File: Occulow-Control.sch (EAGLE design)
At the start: 39 parts, among them T1 DMP3010LK3, T2 DMP3010LK3, T3 DMP3010LK3

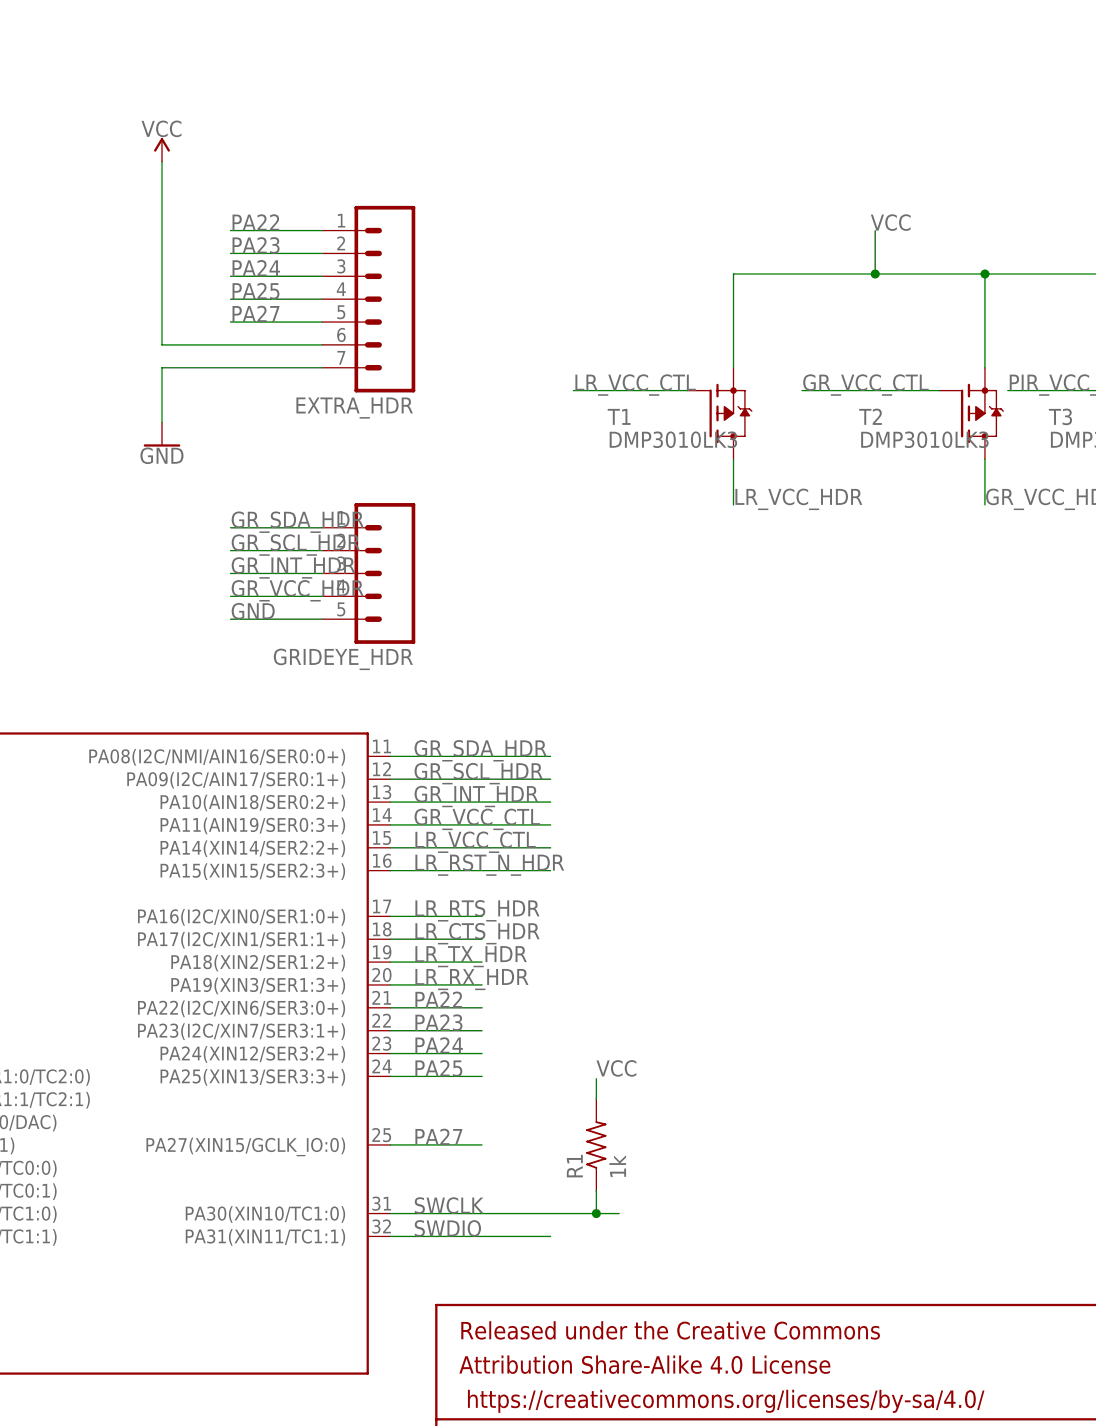
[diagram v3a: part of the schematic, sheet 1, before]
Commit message: Added LED status, bom. Fixes #6"
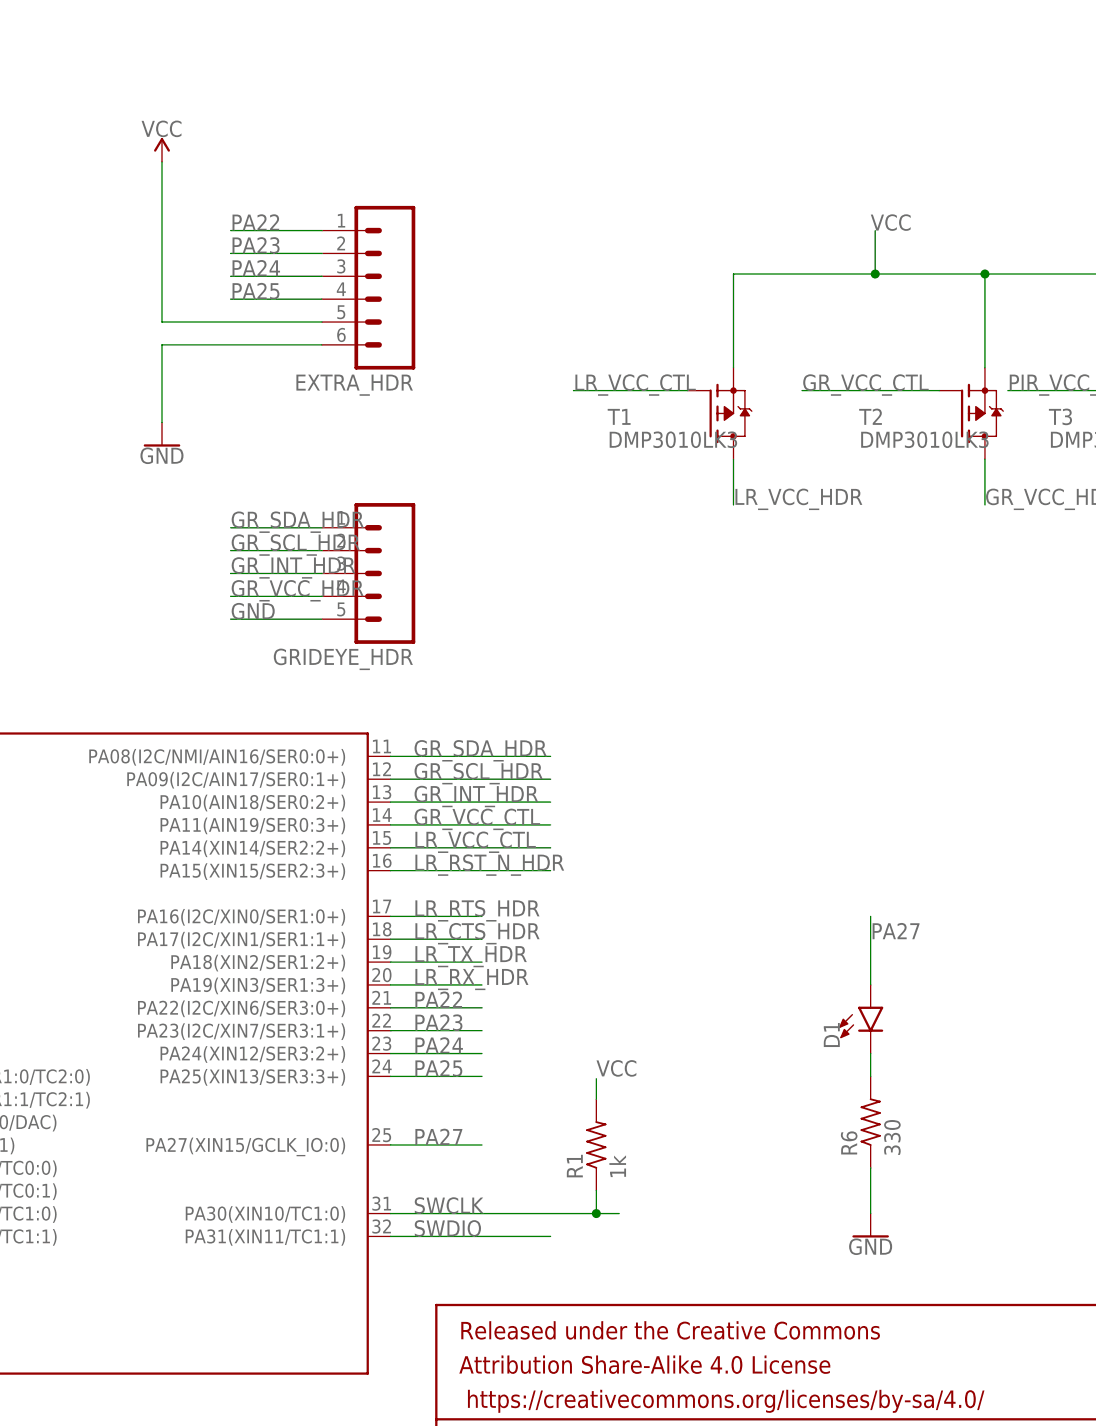
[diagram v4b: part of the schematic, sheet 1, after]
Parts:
- added D1: (no value), SparkFun-LED:LED1206
- added R6: 330, resistor:R-US_R1206
- EXTRA_HDR: device con-amp-quick:M07 -> con-amp-quick:M06
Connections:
- new net N$1: D1.C, R6.2
- net GND: now also EXTRA_HDR.6, R6.1; no longer EXTRA_HDR.7
- net PA27: now also D1.A; no longer EXTRA_HDR.5
- net VCC: now also EXTRA_HDR.5; no longer EXTRA_HDR.6
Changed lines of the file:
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@@
 <part name="SUPPLY6" library="SparkFun-PowerSymbols" deviceset="VCC" device=""/>
 <part name="GND11" library="SparkFun-PowerSymbols" deviceset="GND" device=""/>
-<part name="EXTRA_HDR" library="con-amp-quick" deviceset="M07" device=""/>
+<part name="EXTRA_HDR" library="con-amp-quick" deviceset="M06" device=""/>
 <part name="L1" library="resistor" deviceset="L-US" device="L3225M" value="10uH"/>
 <part name="L2" library="SparkFun-Coils" deviceset="FERRITE_BEAD" device="-0603" value=""/>
@@
 <part name="FRAME3" library="SparkFun-Aesthetics" deviceset="FRAME-LETTER" device="NO_PACKAGE"/>
 <part name="U$5" library="cortex-debug" deviceset="CORTEX-ICE" device=""/>
+<part name="D1" library="SparkFun-LED" deviceset="LED" device="1206"/>
+<part name="R6" library="resistor" deviceset="R-US_" device="R1206" value="330"/>
+<part name="GND5" library="SparkFun-PowerSymbols" deviceset="GND" device=""/>
 </parts>
 <sheets>
@@
 <instance part="LR_CTL_HDR" gate="G$1" x="63.5" y="142.24"/>
 <instance part="U$5" gate="G$1" x="66.04" y="116.84"/>
+<instance part="D1" gate="G$1" x="195.58" y="68.58"/>
+<instance part="R6" gate="G$1" x="195.58" y="55.88" rot="R90"/>
+<instance part="GND5" gate="1" x="195.58" y="43.18"/>
 </instances>
 <busses>
@@
 </segment>
 <segment>
-<pinref part="EXTRA_HDR" gate="G$1" pin="7"/>
 <pinref part="GND10" gate="1" pin="GND"/>
-<wire x1="134.62" y1="139.7" x2="116.84" y2="139.7" width="0.1524" layer="91"/>
-<wire x1="116.84" y1="139.7" x2="116.84" y2="133.604" width="0.1524" layer="91"/>
+<wire x1="116.84" y1="142.24" x2="116.84" y2="133.604" width="0.1524" layer="91"/>
+<pinref part="EXTRA_HDR" gate="G$1" pin="6"/>
+<wire x1="134.62" y1="142.24" x2="116.84" y2="142.24" width="0.1524" layer="91"/>
 </segment>
 <segment>
@@
 <wire x1="68.58" y1="152.4" x2="76.2" y2="152.4" width="0.1524" layer="91"/>
 <label x="68.58" y="152.4" size="1.778" layer="95"/>
+</segment>
+<segment>
+<pinref part="GND5" gate="1" pin="GND"/>
+<pinref part="R6" gate="G$1" pin="1"/>
+<wire x1="195.58" y1="45.72" x2="195.58" y2="50.8" width="0.1524" layer="91"/>
 </segment>
 </net>
@@
 </segment>
 <segment>
-<pinref part="SUPPLY5" gate="G$1" pin="VCC"/>
-<wire x1="116.84" y1="142.24" x2="116.84" y2="162.56" width="0.1524" layer="91"/>
-<pinref part="EXTRA_HDR" gate="G$1" pin="6"/>
-<wire x1="134.62" y1="142.24" x2="116.84" y2="142.24" width="0.1524" layer="91"/>
-</segment>
-<segment>
 <pinref part="R1" gate="G$1" pin="2"/>
 <wire x1="165.1" y1="60.706" x2="165.1" y2="58.42" width="0.1524" layer="91"/>
@@
 <label x="195.58" y="154.94" size="1.778" layer="95"/>
 </segment>
+<segment>
+<pinref part="EXTRA_HDR" gate="G$1" pin="5"/>
+<pinref part="SUPPLY5" gate="G$1" pin="VCC"/>
+<wire x1="134.62" y1="144.78" x2="116.84" y2="144.78" width="0.1524" layer="91"/>
+<wire x1="116.84" y1="144.78" x2="116.84" y2="162.56" width="0.1524" layer="91"/>
+</segment>
 </net>
 <net name="LR_VCC_CTL" class="0">
@@
 </segment>
 <segment>
-<pinref part="EXTRA_HDR" gate="G$1" pin="5"/>
-<wire x1="134.62" y1="144.78" x2="124.46" y2="144.78" width="0.1524" layer="91"/>
-<label x="124.46" y="144.78" size="1.778" layer="95"/>
+<pinref part="D1" gate="G$1" pin="A"/>
+<wire x1="195.58" y1="71.12" x2="195.58" y2="78.74" width="0.1524" layer="91"/>
+<label x="195.58" y="76.2" size="1.778" layer="95"/>
 </segment>
 </net>
@@
 </segment>
 </net>
+<net name="N$1" class="0">
+<segment>
+<pinref part="R6" gate="G$1" pin="2"/>
+<pinref part="D1" gate="G$1" pin="C"/>
+<wire x1="195.58" y1="60.96" x2="195.58" y2="63.5" width="0.1524" layer="91"/>
+</segment>
+</net>
